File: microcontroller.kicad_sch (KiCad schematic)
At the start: 43 parts, among them J1 Conn_01x02, J3 SWD, SW1 SW_SPDT, U1 STM32F105RCTx, U2 SN65HVD230, U4 CD143A-SR05, Y1 16MHz

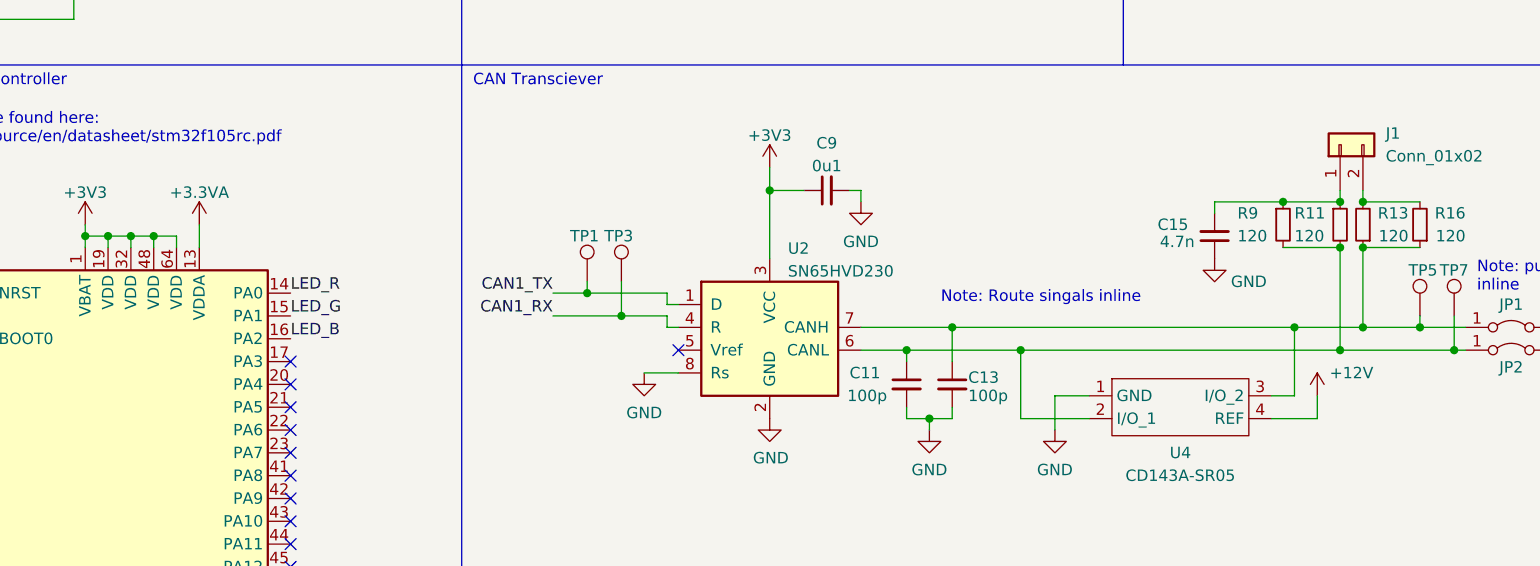
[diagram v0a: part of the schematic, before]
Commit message: Adjusted CAN bus voltage to 5V
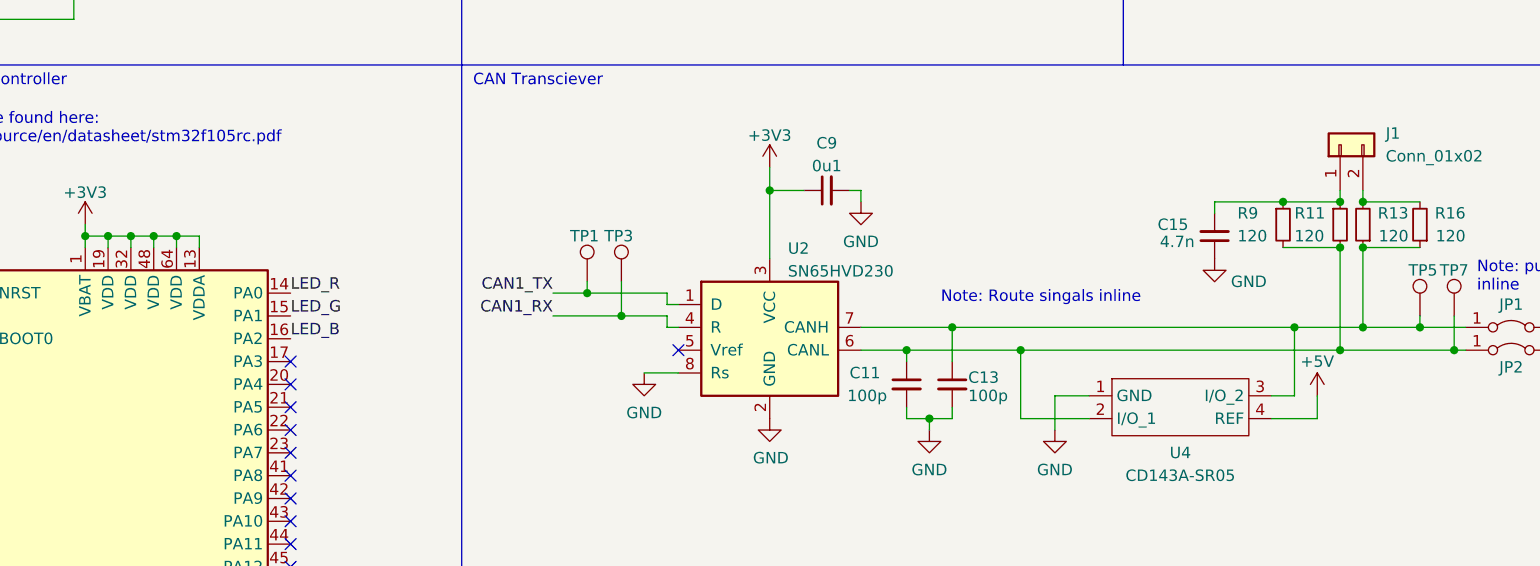
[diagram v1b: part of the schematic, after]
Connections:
- net +3.3VA: no longer U1.13 (VDDA)
- net +3V3: now also U1.13 (VDDA)
- net +12V renamed +5V
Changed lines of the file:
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@@
   (junction (at 142.24 185.42) (diameter 0) (color 0 0 0 0)
+  )
+  (junction (at 54.61 92.71) (diameter 0) (color 0 0 0 0)
   )
   (junction (at 177.8 88.9) (diameter 0) (color 0 0 0 0)
@@
     (stroke (width 0) (type default) (color 0 0 0 0))
   )
+  (wire (pts (xy 57.15 93.98) (xy 57.15 92.71))
+    (stroke (width 0) (type default) (color 0 0 0 0))
+  )
   (wire (pts (xy 142.24 190.5) (xy 143.51 190.5))
     (stroke (width 0) (type default) (color 0 0 0 0))
@@
     (stroke (width 0) (type default) (color 0 0 0 0))
   )
+  (wire (pts (xy 57.15 92.71) (xy 54.61 92.71))
+    (stroke (width 0) (type default) (color 0 0 0 0))
+  )
   (wire (pts (xy 119.38 46.99) (xy 119.38 48.26))
     (stroke (width 0) (type default) (color 0 0 0 0))
@@
   )
   (wire (pts (xy 96.52 101.6) (xy 104.14 101.6))
-    (stroke (width 0) (type default) (color 0 0 0 0))
-  )
-  (wire (pts (xy 57.15 91.44) (xy 57.15 93.98))
     (stroke (width 0) (type default) (color 0 0 0 0))
   )
@@
     (pin "1")
   )
-  (symbol (lib_id "power:+3.3VA") (at 57.15 91.44 0) (unit 1)
-    (in_bom yes) (on_board yes) (fields_autoplaced)
-    (property "Reference" "#PWR07" (id 0) (at 57.15 95.25 0)
-      (effects (font (size 1.27 1.27)) hide)
-    )
-    (property "Value" "+3.3VA" (id 1) (at 57.15 87.8642 0))
-    (property "Footprint" "" (id 2) (at 57.15 91.44 0)
-      (effects (font (size 1.27 1.27)) hide)
-    )
-    (property "Datasheet" "" (id 3) (at 57.15 91.44 0)
-      (effects (font (size 1.27 1.27)) hide)
-    )
-    (pin "1")
-  )
   (symbol (lib_id "power:GND") (at 152.4 114.3 0) (unit 1)
     (in_bom yes) (on_board yes) (fields_autoplaced)
@@
     )
     (property "Datasheet" "" (id 3) (at 152.4 114.3 0)
-      (effects (font (size 1.27 1.27)) hide)
-    )
-    (pin "1")
-  )
-  (symbol (lib_id "power:+12V") (at 181.61 110.49 0) (unit 1)
-    (in_bom yes) (on_board yes)
-    (property "Reference" "#PWR031" (id 0) (at 181.61 114.3 0)
-      (effects (font (size 1.27 1.27)) hide)
-    )
-    (property "Value" "+12V" (id 1) (at 185.42 107.95 0))
-    (property "Footprint" "" (id 2) (at 181.61 110.49 0)
-      (effects (font (size 1.27 1.27)) hide)
-    )
-    (property "Datasheet" "" (id 3) (at 181.61 110.49 0)
       (effects (font (size 1.27 1.27)) hide)
     )
@@
     (pin "2")
   )
+  (symbol (lib_id "power:+5V") (at 181.61 110.49 0) (unit 1)
+    (in_bom yes) (on_board yes)
+    (property "Reference" "#PWR?" (id 0) (at 181.61 114.3 0)
+      (effects (font (size 1.27 1.27)) hide)
+    )
+    (property "Value" "+5V" (id 1) (at 181.61 106.68 0))
+    (property "Footprint" "" (id 2) (at 181.61 110.49 0)
+      (effects (font (size 1.27 1.27)) hide)
+    )
+    (property "Datasheet" "" (id 3) (at 181.61 110.49 0)
+      (effects (font (size 1.27 1.27)) hide)
+    )
+    (pin "1")
+  )
   (symbol (lib_id "power:+3V3") (at 138.43 184.15 0) (unit 1)

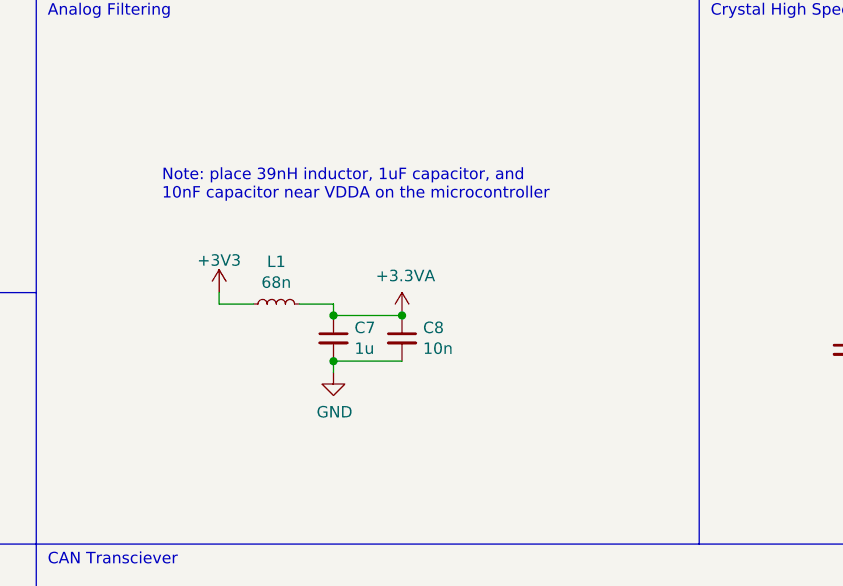
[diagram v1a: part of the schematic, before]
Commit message: Removed analog filtering
There are no analog parts in this PCB
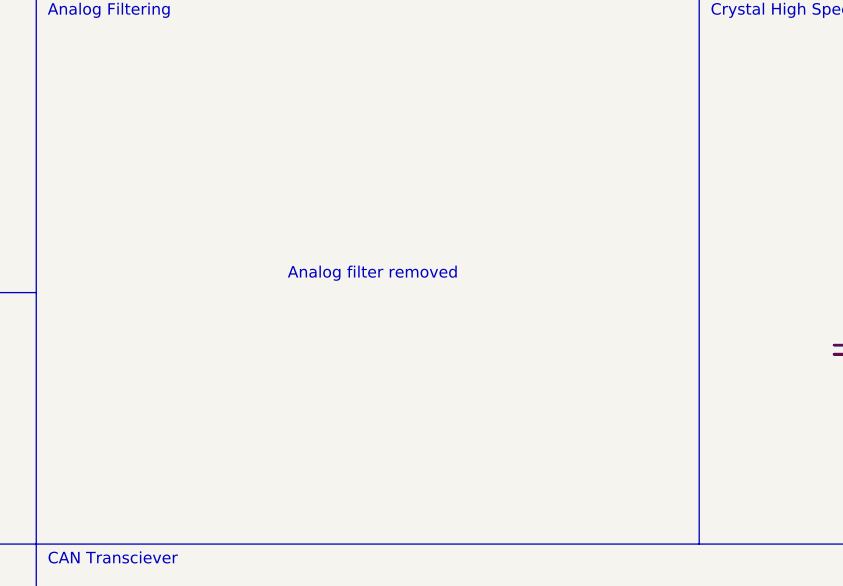
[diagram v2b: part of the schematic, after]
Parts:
- removed C7: 1u, Capacitor_SMD:C_0603_1608Metric, symbol Device:C_Small
- removed C8: 10n, Capacitor_SMD:C_0603_1608Metric, symbol Device:C_Small
- removed L1: 68n, Inductor_SMD:L_0603_1608Metric, symbol Device:L_Small
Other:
- note added: "Analog filter removed"
- note removed: "Note: place 39nH inductor, 1uF capacitor, and 10nF capacitor near VDDA on the microcontroller"
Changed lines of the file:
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@@
   (junction (at 184.15 57.15) (diameter 0) (color 0 0 0 0)
   )
-  (junction (at 119.38 53.34) (diameter 0) (color 0 0 0 0)
-  )
   (junction (at 60.96 35.56) (diameter 0) (color 0 0 0 0)
   )
@@
   (junction (at 176.53 46.99) (diameter 0) (color 0 0 0 0)
   )
-  (junction (at 119.38 48.26) (diameter 0) (color 0 0 0 0)
-  )
   (junction (at 193.04 102.87) (diameter 0) (color 0 0 0 0)
   )
@@
   )
   (junction (at 44.45 92.71) (diameter 0) (color 0 0 0 0)
-  )
-  (junction (at 127 48.26) (diameter 0) (color 0 0 0 0)
   )
   (junction (at 236.22 92.71) (diameter 0) (color 0 0 0 0)
@@
   (no_connect (at 250.19 149.86))
   (no_connect (at 110.49 105.41))
-  (wire (pts (xy 106.68 45.72) (xy 106.68 46.99))
-    (stroke (width 0) (type default) (color 0 0 0 0))
-  )
   (wire (pts (xy 152.4 110.49) (xy 152.4 114.3))
     (stroke (width 0) (type default) (color 0 0 0 0))
@@
     (stroke (width 0) (type default) (color 0 0 0 0))
   )
-  (wire (pts (xy 106.68 46.99) (xy 110.49 46.99))
-    (stroke (width 0) (type default) (color 0 0 0 0))
-  )
-  (wire (pts (xy 127 53.34) (xy 119.38 53.34))
-    (stroke (width 0) (type default) (color 0 0 0 0))
-  )
   (wire (pts (xy 57.15 93.98) (xy 57.15 92.71))
     (stroke (width 0) (type default) (color 0 0 0 0))
@@
     (stroke (width 0) (type default) (color 0 0 0 0))
   )
-  (wire (pts (xy 119.38 53.34) (xy 119.38 54.61))
-    (stroke (width 0) (type default) (color 0 0 0 0))
-  )
   (wire (pts (xy 193.04 102.87) (xy 198.12 102.87))
     (stroke (width 0) (type default) (color 0 0 0 0))
@@
     (stroke (width 0) (type default) (color 0 0 0 0))
   )
-  (wire (pts (xy 119.38 46.99) (xy 119.38 48.26))
-    (stroke (width 0) (type default) (color 0 0 0 0))
-  )
   (wire (pts (xy 130.81 105.41) (xy 135.89 105.41))
     (stroke (width 0) (type default) (color 0 0 0 0))
@@
     (stroke (width 0) (type default) (color 0 0 0 0))
   )
-  (wire (pts (xy 119.38 48.26) (xy 127 48.26))
-    (stroke (width 0) (type default) (color 0 0 0 0))
-  )
   (wire (pts (xy 109.22 101.6) (xy 109.22 102.87))
     (stroke (width 0) (type default) (color 0 0 0 0))
@@
   )
   (wire (pts (xy 44.45 92.71) (xy 46.99 92.71))
-    (stroke (width 0) (type default) (color 0 0 0 0))
-  )
-  (wire (pts (xy 115.57 46.99) (xy 119.38 46.99))
     (stroke (width 0) (type default) (color 0 0 0 0))
   )
@@
     (effects (font (size 1.27 1.27)) (justify left bottom))
   )
-  (text "Note: place 39nH inductor, 1uF capacitor, and \n10nF capacitor near VDDA on the microcontroller"
-    (at 100.33 35.56 0)
+  (text "Analog filter removed" (at 114.3 44.45 0)
     (effects (font (size 1.27 1.27)) (justify left bottom))
   )
@@
     (pin "1")
   )
-  (symbol (lib_id "Device:L_Small") (at 113.03 46.99 90) (unit 1)
-    (in_bom yes) (on_board yes)
-    (property "Reference" "L1" (id 0) (at 113.03 42.291 90))
-    (property "Value" "68n" (id 1) (at 113.03 44.6024 90))
-    (property "Footprint" "Inductor_SMD:L_0603_1608Metric" (id 2) (at 113.03 46.99 0)
-      (effects (font (size 1.27 1.27)) hide)
-    )
-    (property "Datasheet" "~" (id 3) (at 113.03 46.99 0)
-      (effects (font (size 1.27 1.27)) hide)
-    )
-    (pin "1")
-    (pin "2")
-  )
-  (symbol (lib_id "power:+3.3VA") (at 127 48.26 0) (unit 1)
-    (in_bom yes) (on_board yes)
-    (property "Reference" "#PWR020" (id 0) (at 127 52.07 0)
-      (effects (font (size 1.27 1.27)) hide)
-    )
-    (property "Value" "+3.3VA" (id 1) (at 127.381 43.8658 0))
-    (property "Footprint" "" (id 2) (at 127 48.26 0)
-      (effects (font (size 1.27 1.27)) hide)
-    )
-    (property "Datasheet" "" (id 3) (at 127 48.26 0)
-      (effects (font (size 1.27 1.27)) hide)
-    )
-    (pin "1")
-  )
-  (symbol (lib_id "Device:C_Small") (at 119.38 50.8 0) (unit 1)
-    (in_bom yes) (on_board yes)
-    (property "Reference" "C7" (id 0) (at 121.7168 49.6316 0)
-      (effects (font (size 1.27 1.27)) (justify left))
-    )
-    (property "Value" "1u" (id 1) (at 121.7168 51.943 0)
-      (effects (font (size 1.27 1.27)) (justify left))
-    )
-    (property "Footprint" "Capacitor_SMD:C_0603_1608Metric" (id 2) (at 119.38 50.8 0)
-      (effects (font (size 1.27 1.27)) hide)
-    )
-    (property "Datasheet" "~" (id 3) (at 119.38 50.8 0)
-      (effects (font (size 1.27 1.27)) hide)
-    )
-    (pin "1")
-    (pin "2")
-  )
-  (symbol (lib_id "Device:C_Small") (at 127 50.8 0) (unit 1)
-    (in_bom yes) (on_board yes)
-    (property "Reference" "C8" (id 0) (at 129.3368 49.6316 0)
-      (effects (font (size 1.27 1.27)) (justify left))
-    )
-    (property "Value" "10n" (id 1) (at 129.3368 51.943 0)
-      (effects (font (size 1.27 1.27)) (justify left))
-    )
-    (property "Footprint" "Capacitor_SMD:C_0603_1608Metric" (id 2) (at 127 50.8 0)
-      (effects (font (size 1.27 1.27)) hide)
-    )
-    (property "Datasheet" "~" (id 3) (at 127 50.8 0)
-      (effects (font (size 1.27 1.27)) hide)
-    )
-    (pin "1")
-    (pin "2")
-  )
-  (symbol (lib_id "power:GND") (at 119.38 54.61 0) (unit 1)
-    (in_bom yes) (on_board yes)
-    (property "Reference" "#PWR015" (id 0) (at 119.38 60.96 0)
-      (effects (font (size 1.27 1.27)) hide)
-    )
-    (property "Value" "GND" (id 1) (at 119.507 59.0042 0))
-    (property "Footprint" "" (id 2) (at 119.38 54.61 0)
-      (effects (font (size 1.27 1.27)) hide)
-    )
-    (property "Datasheet" "" (id 3) (at 119.38 54.61 0)
-      (effects (font (size 1.27 1.27)) hide)
-    )
-    (pin "1")
-  )
   (symbol (lib_id "Device:Crystal_GND24_Small") (at 184.15 46.99 0) (unit 1)
     (in_bom yes) (on_board yes)
@@
       (effects (font (size 1.27 1.27)) hide)
     )
-    (pin "1")
-  )
-  (symbol (lib_id "power:+3V3") (at 106.68 45.72 0) (unit 1)
-    (in_bom yes) (on_board yes) (fields_autoplaced)
-    (property "Reference" "#PWR011" (id 0) (at 106.68 49.53 0)
-      (effects (font (size 1.27 1.27)) hide)
-    )
-    (property "Value" "+3V3" (id 1) (at 106.68 42.1442 0))
-    (property "Footprint" "" (id 2) (at 106.68 45.72 0)
-      (effects (font (size 1.27 1.27)) hide)
-    )
-    (property "Datasheet" "" (id 3) (at 106.68 45.72 0)
-      (effects (font (size 1.27 1.27)) hide)
-    )

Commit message: Annotated schematic
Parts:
- renumbered C11 to C10, C13 to C11, C15 to C12, C17 to C13, C18 to C14, C1 to C3, C2 to C4, C3 to C5, C4 to C6, C5 to C7, C6 to C8, J1 to J4, J3 to J5, R13 to R10, R15 to R11, R16 to R12, R18 to R13, R19 to R14, R1 to R2, R2 to R3, R5 to R4, R6 to R5, R7 to R6, R8 to R7, R9 to R8, R11 to R9, TP3 to TP2, TP5 to TP3, TP7 to TP4, U1 to U2, U2 to U3
